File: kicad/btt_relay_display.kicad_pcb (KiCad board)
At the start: 2 copper layers, 30 x 20 mm, 19 parts, among them J1 RELAY, J2 PROGRAM, Q1 BC847, Q2 BC847, SW1 RESET

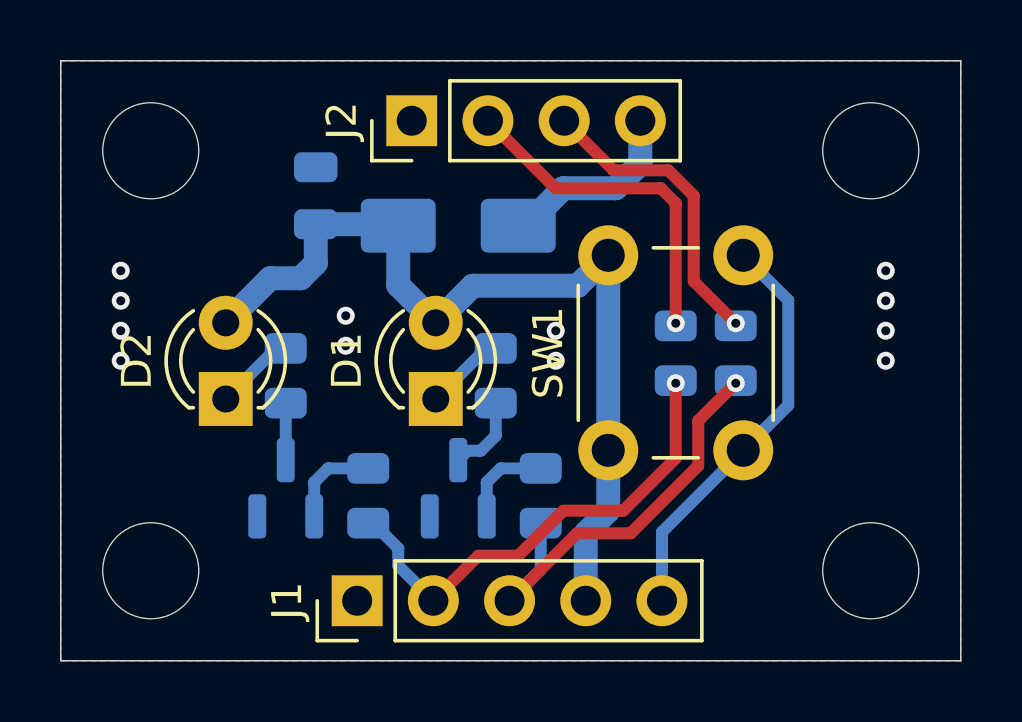
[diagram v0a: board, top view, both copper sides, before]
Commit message: Update PCB to include OHW logo and position reference text properly.
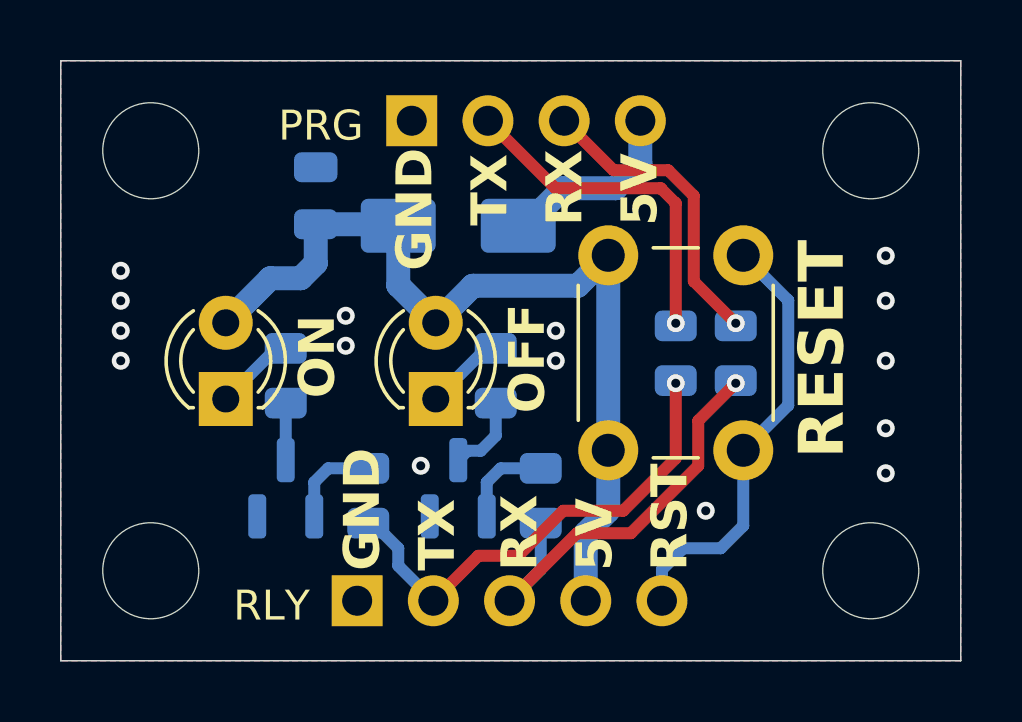
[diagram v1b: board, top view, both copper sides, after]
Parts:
- added REF**: OSHW-Logo2_7.3x6mm_SilkScreen, Symbol:OSHW-Logo2_7.3x6mm_SilkScreen, B.Cu at (166.5, 80.0)
- J1, J2: moved to B.Cu
- turned J1 to -90 degrees
- turned J2 to -90 degrees
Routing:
- net /RST: track 13.9 -> 14.6 mm
- net GND: vias 12 -> 15
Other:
- board text added: "5V"
- board text added: "GND"
- board text added: "OFF"
- board text added: "ON"
- board text added: "PRG"
- board text added: "RESET"
- board text added: "RLY"
- board text added: "RST"
- board text added: "RX"
- board text added: "TX"

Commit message: Holes made 2.5mm add pcb name text, generate gerbes for jlcpcb assembly service
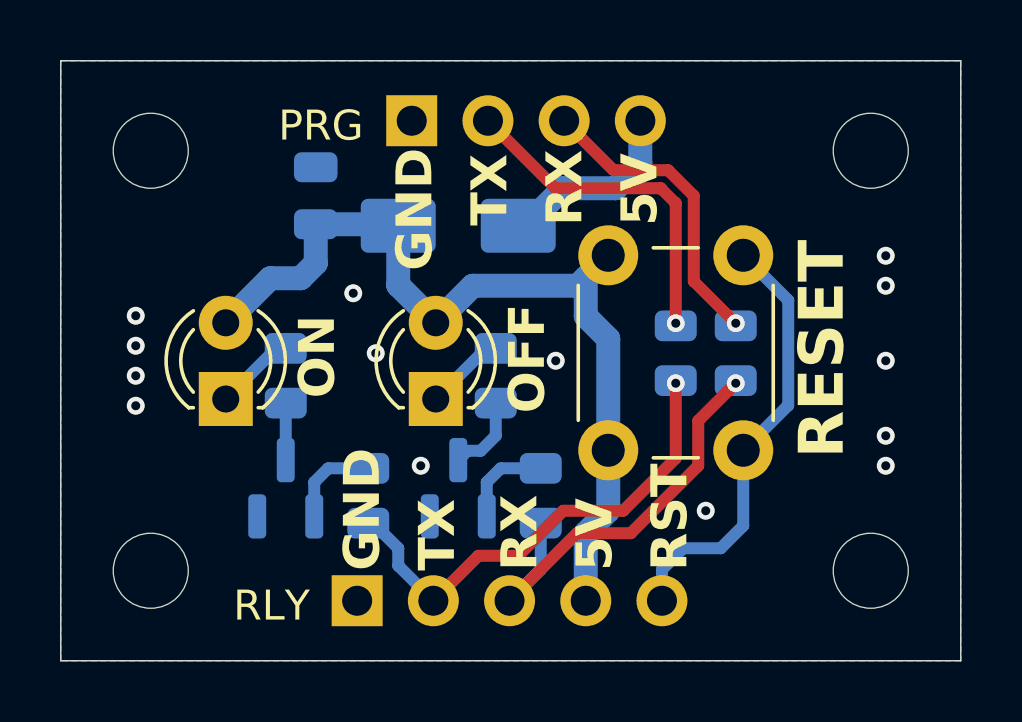
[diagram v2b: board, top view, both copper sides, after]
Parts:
- removed the REF** at (143.0, 73.0)
- removed the REF** at (143.0, 87.0)
- removed the REF** at (167.0, 87.0)
- removed the REF** at (167.0, 73.0)
- added REF**: MountingHole_2.5mm, MountingHole:MountingHole_2.5mm, F.Cu at (143.0, 73.0)
- added REF**: MountingHole_2.5mm, MountingHole:MountingHole_2.5mm, F.Cu at (167.0, 87.0)
- added REF**: MountingHole_2.5mm, MountingHole:MountingHole_2.5mm, F.Cu at (167.0, 73.0)
- added REF**: MountingHole_2.5mm, MountingHole:MountingHole_2.5mm, F.Cu at (143.0, 87.0)
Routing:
- net /5V: track 30.2 -> 30.8 mm
- net GND: vias 15 -> 14
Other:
- board text added: "BTT RELAY"
- board text added: "DISPLAY"
